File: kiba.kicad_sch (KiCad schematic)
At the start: 7 parts, among them J1 Raspberry_Pi_2_3, U1 LM1117MP-3.3

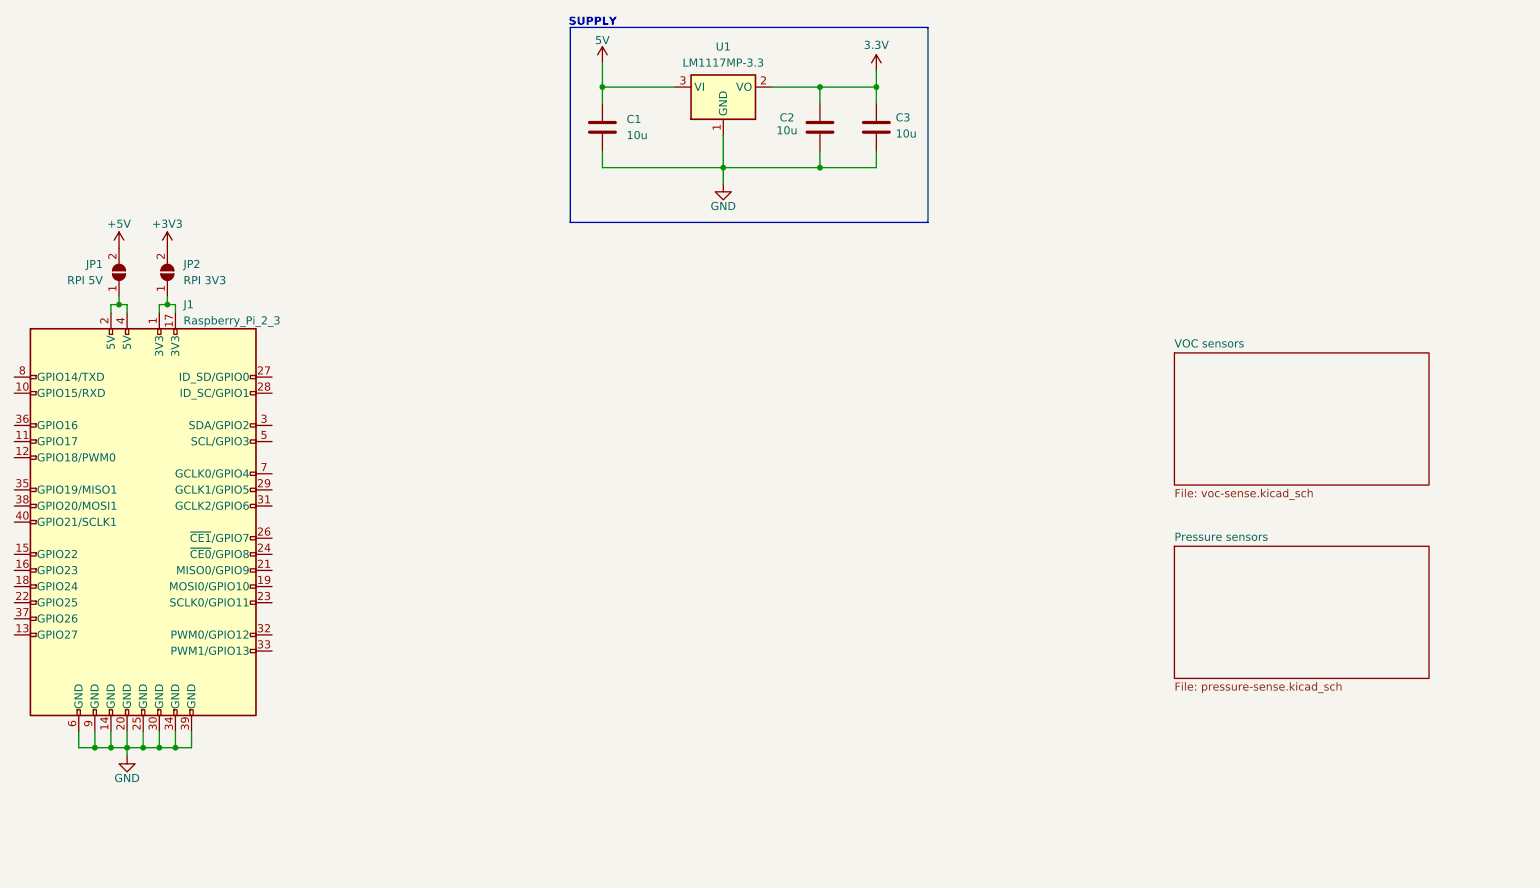
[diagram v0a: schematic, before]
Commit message: fix: bmp581 config
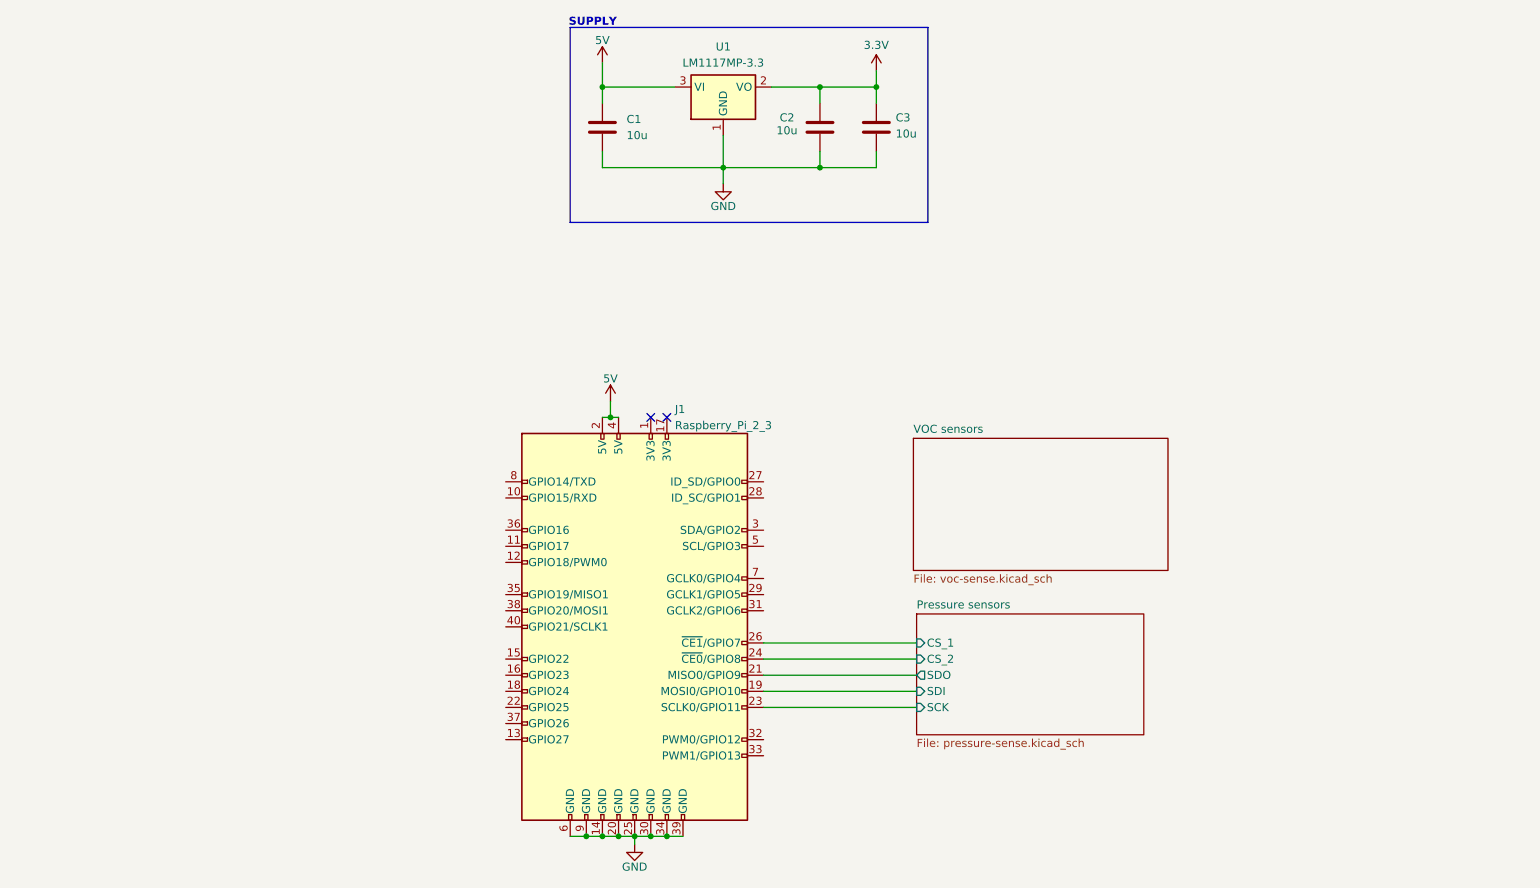
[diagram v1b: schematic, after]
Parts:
- removed JP1: RPI 5V, Jumper:SolderJumper-2_P1.3mm_Open_RoundedPad1.0x1.5mm, symbol Jumper:SolderJumper_2_Open
- removed JP2: RPI 3V3, Jumper:SolderJumper-2_P1.3mm_Open_RoundedPad1.0x1.5mm, symbol Jumper:SolderJumper_2_Open
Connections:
- net 5V: now also J1.2 (5V), J1.4 (5V)
- net at J1.1 (3V3): no longer J1.17 (3V3)
- net Pressure sensors/SDI: now reaches J1.19 (MOSI0/GPIO10)
- net Pressure sensors/SDO: now reaches J1.21 (MISO0/GPIO9)
- net Pressure sensors/SCK: now reaches J1.23 (SCLK0/GPIO11)
- net Pressure sensors/CS_2: now reaches J1.24 (~{CE0}/GPIO8)
- net Pressure sensors/CS_1: now reaches J1.26 (~{CE1}/GPIO7)
- no-connect marks 0 -> 2
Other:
- sheet Pressure sensors ports: added CS_1, CS_2, SCK, SDI, SDO; removed none
- moved on the sheet: J1

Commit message: feat: add buzzer
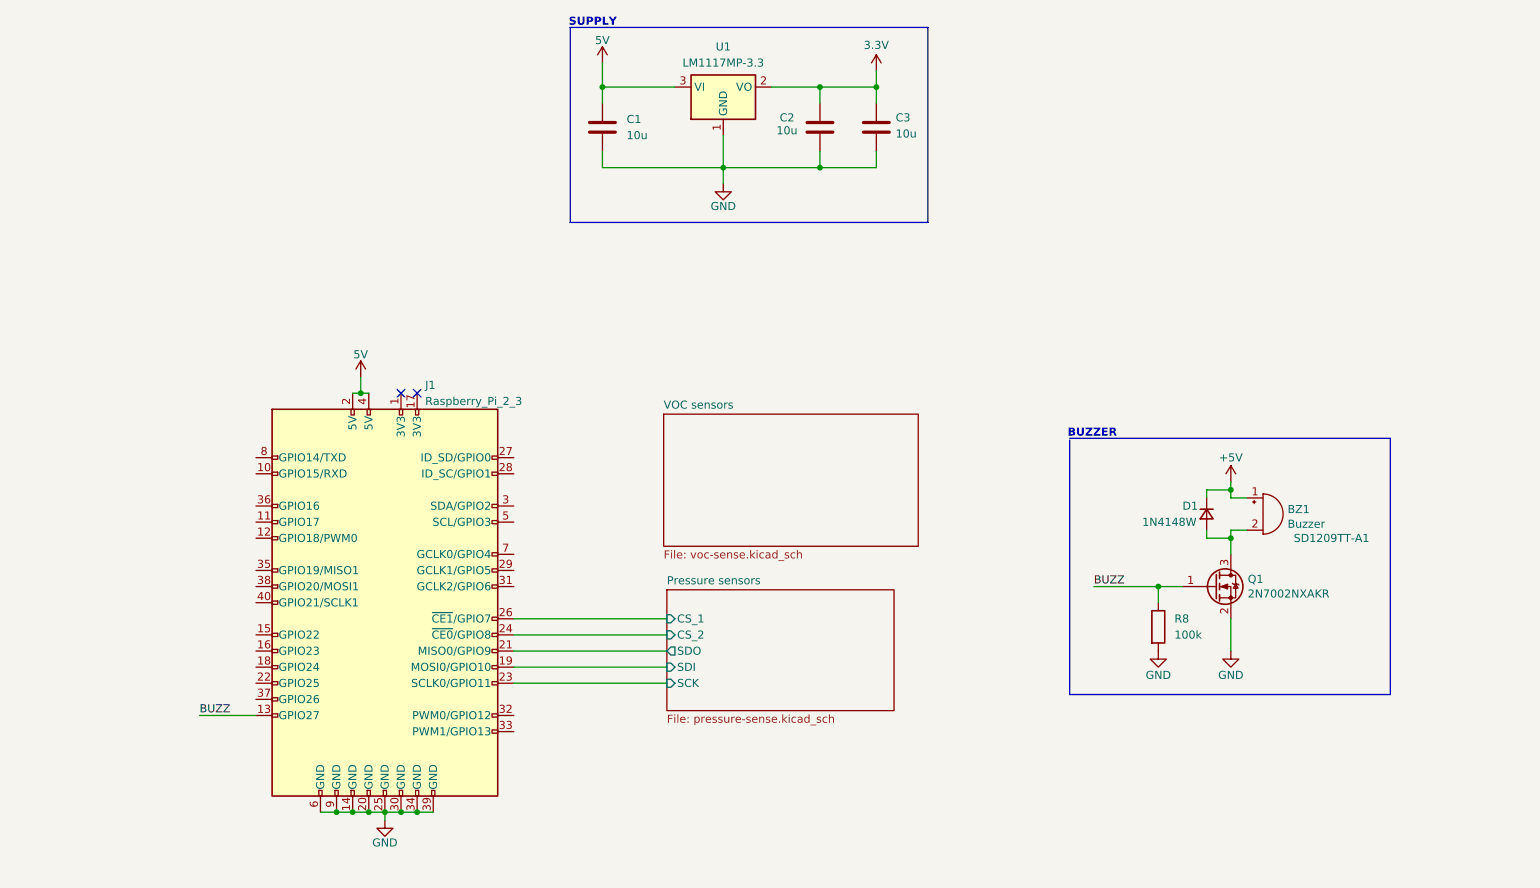
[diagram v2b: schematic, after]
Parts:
- added BZ1: Buzzer, Buzzer_Beeper:Buzzer_TDK_PS1240P02BT_D12.2mm_H6.5mm, symbol Device:Buzzer
- added D1: 1N4148W, Diode_SMD:D_SOD-323_HandSoldering, symbol Device:D_Small
- added Q1: 2N7002NXAKR, Package_TO_SOT_SMD:SOT-23, symbol Device:Q_NMOS_GSD
- added R8: 100k, Resistor_SMD:R_0603_1608Metric, symbol Device:R
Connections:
- net GND: now also Q1.2 (S), R8.2
- net BUZZ: now reaches J1.13 (GPIO27)
- net BUZZ: now also Q1.1 (G), R8.1
- new net: BZ1.2 (+), D1.2 (A), Q1.3 (D)
- new net +5V: BZ1.1 (-), D1.1 (K)
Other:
- note added: "BUZZER"
- moved on the sheet: J1

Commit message: feat: new configuration with i2c switch
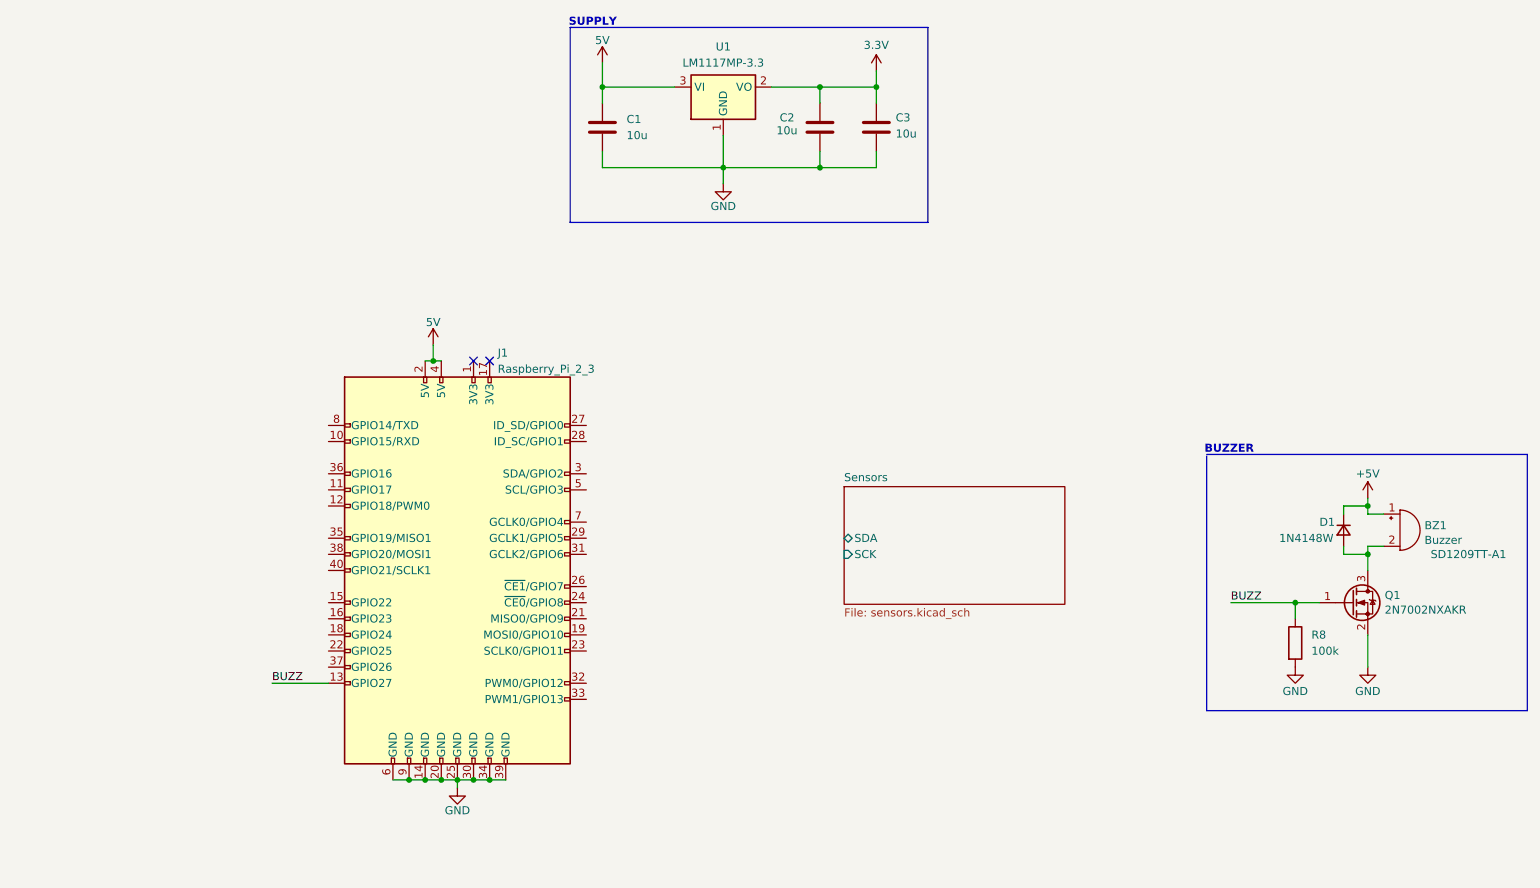
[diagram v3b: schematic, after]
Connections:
- net Pressure sensors/CS_1: no longer names the net of J1.26 (~{CE1}/GPIO7)
- net Pressure sensors/CS_2: no longer names the net of J1.24 (~{CE0}/GPIO8)
- net Pressure sensors/SCK: no longer names the net of J1.23 (SCLK0/GPIO11)
- net Pressure sensors/SDI: no longer names the net of J1.19 (MOSI0/GPIO10)
- net Pressure sensors/SDO: no longer names the net of J1.21 (MISO0/GPIO9)
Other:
- removed sheet Pressure sensors
- removed sheet VOC sensors
- added sheet Sensors (sensors.kicad_sch)
- moved on the sheet: BZ1, D1, J1, Q1, R8

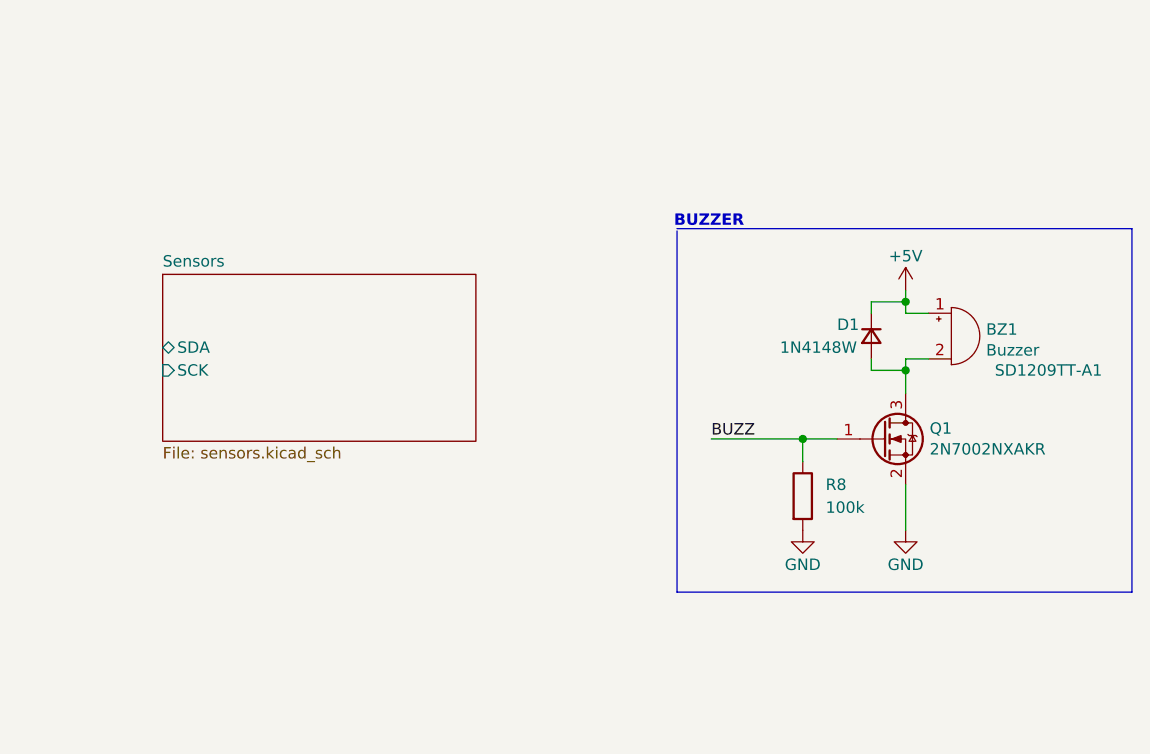
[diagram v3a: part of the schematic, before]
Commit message: feat: address selection i2c switch
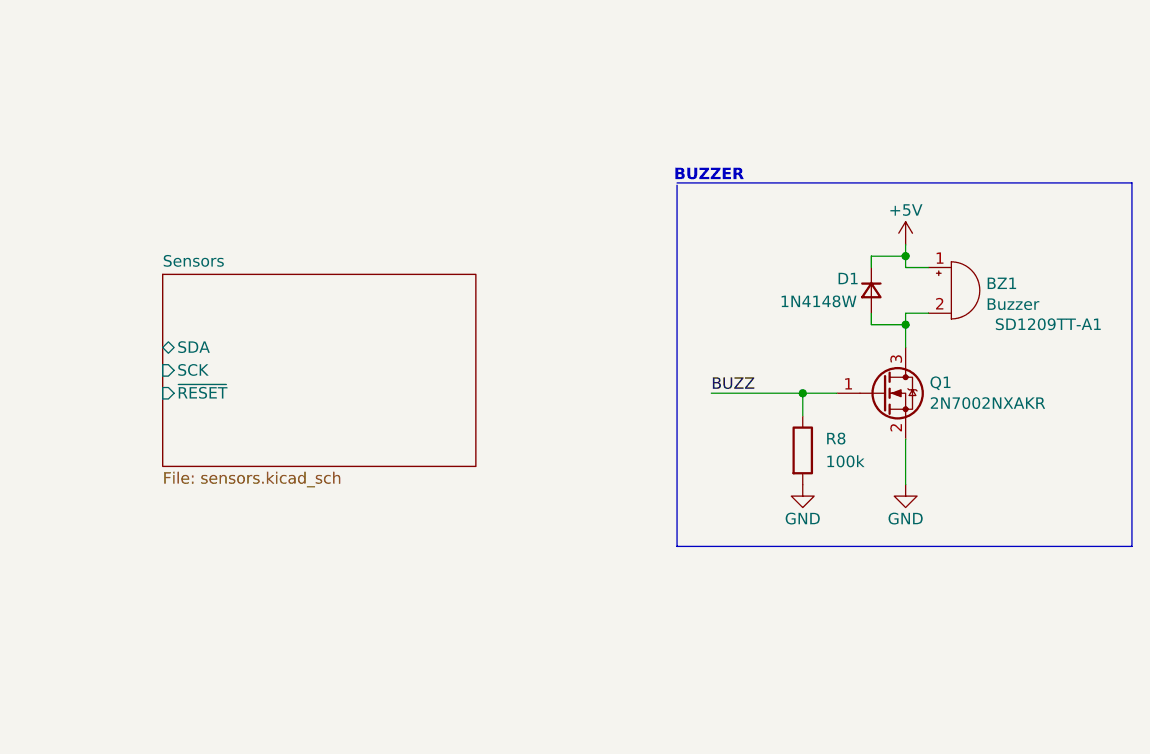
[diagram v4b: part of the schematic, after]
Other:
- sheet Sensors ports: added ~{RESET}; removed none
- moved on the sheet: BZ1, D1, Q1, R8

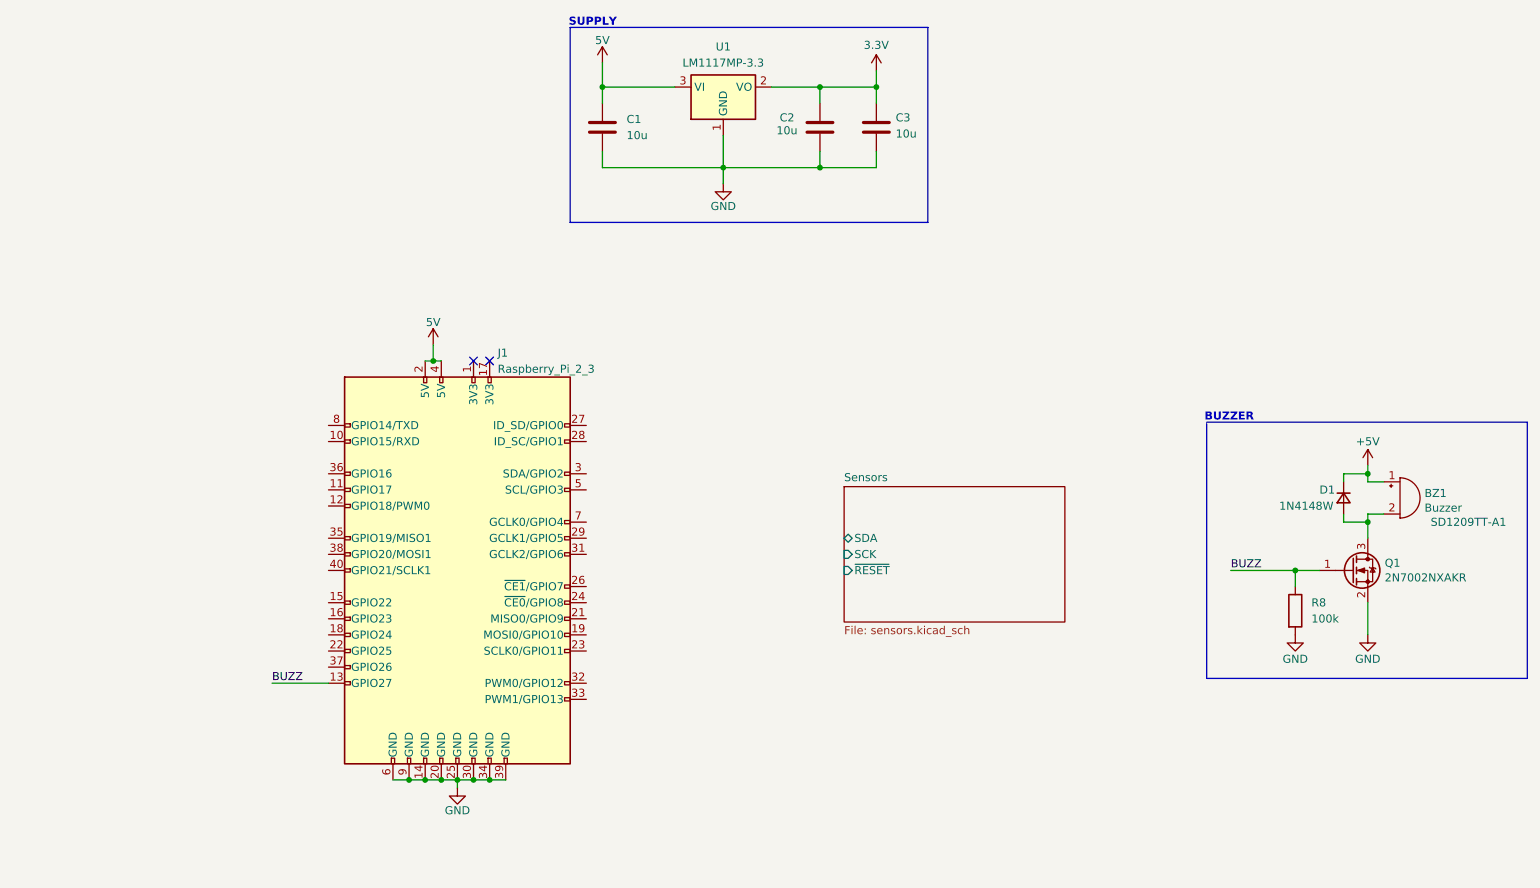
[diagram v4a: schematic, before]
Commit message: feat: rasp connections + fan
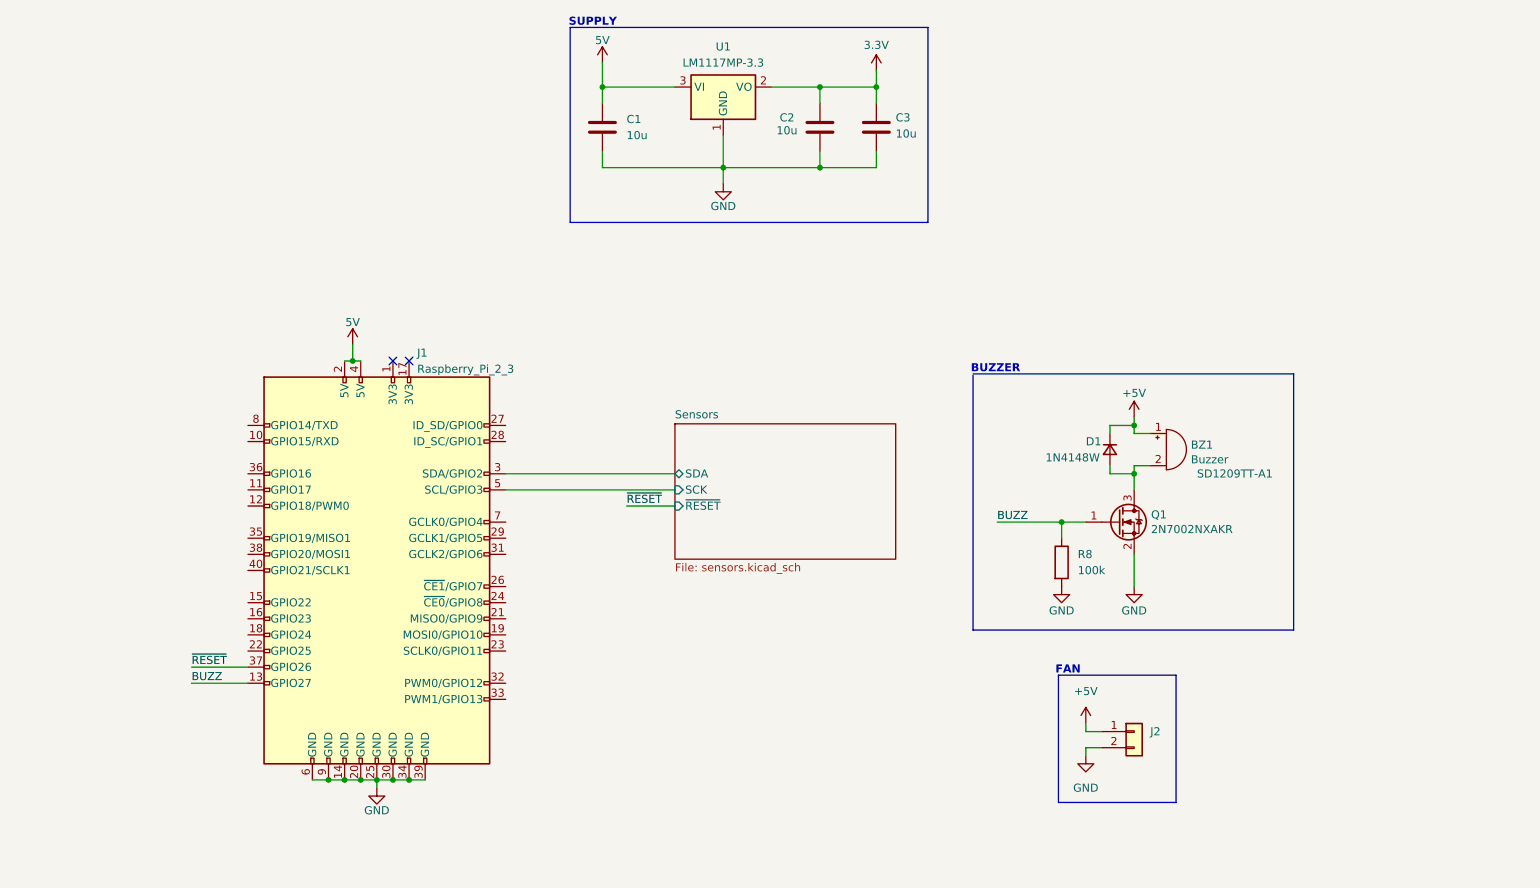
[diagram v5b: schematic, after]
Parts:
- added J2: Conn_01x02, symbol Connector_Generic:Conn_01x02
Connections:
- net +5V: now also J2.1 (Pin_1)
- net GND: now also J2.2 (Pin_2)
- net Sensors/SCK: now also J1.5 (SCL/GPIO3)
- net Sensors/SDA: now also J1.3 (SDA/GPIO2)
- net ~{RESET}: now reaches J1.37 (GPIO26)
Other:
- note added: "FAN"
- moved on the sheet: BZ1, D1, J1, Q1, R8
